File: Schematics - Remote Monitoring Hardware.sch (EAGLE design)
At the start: 48 parts, among them IC1 MSP430G2553, IC2 TPS77001, IC3 Xbee S3 Socket, IC4 MAX31855T, J5B PCC-SMP, J7 53047-06, Q1 32.768kHz, Q2 DMP3099L-7

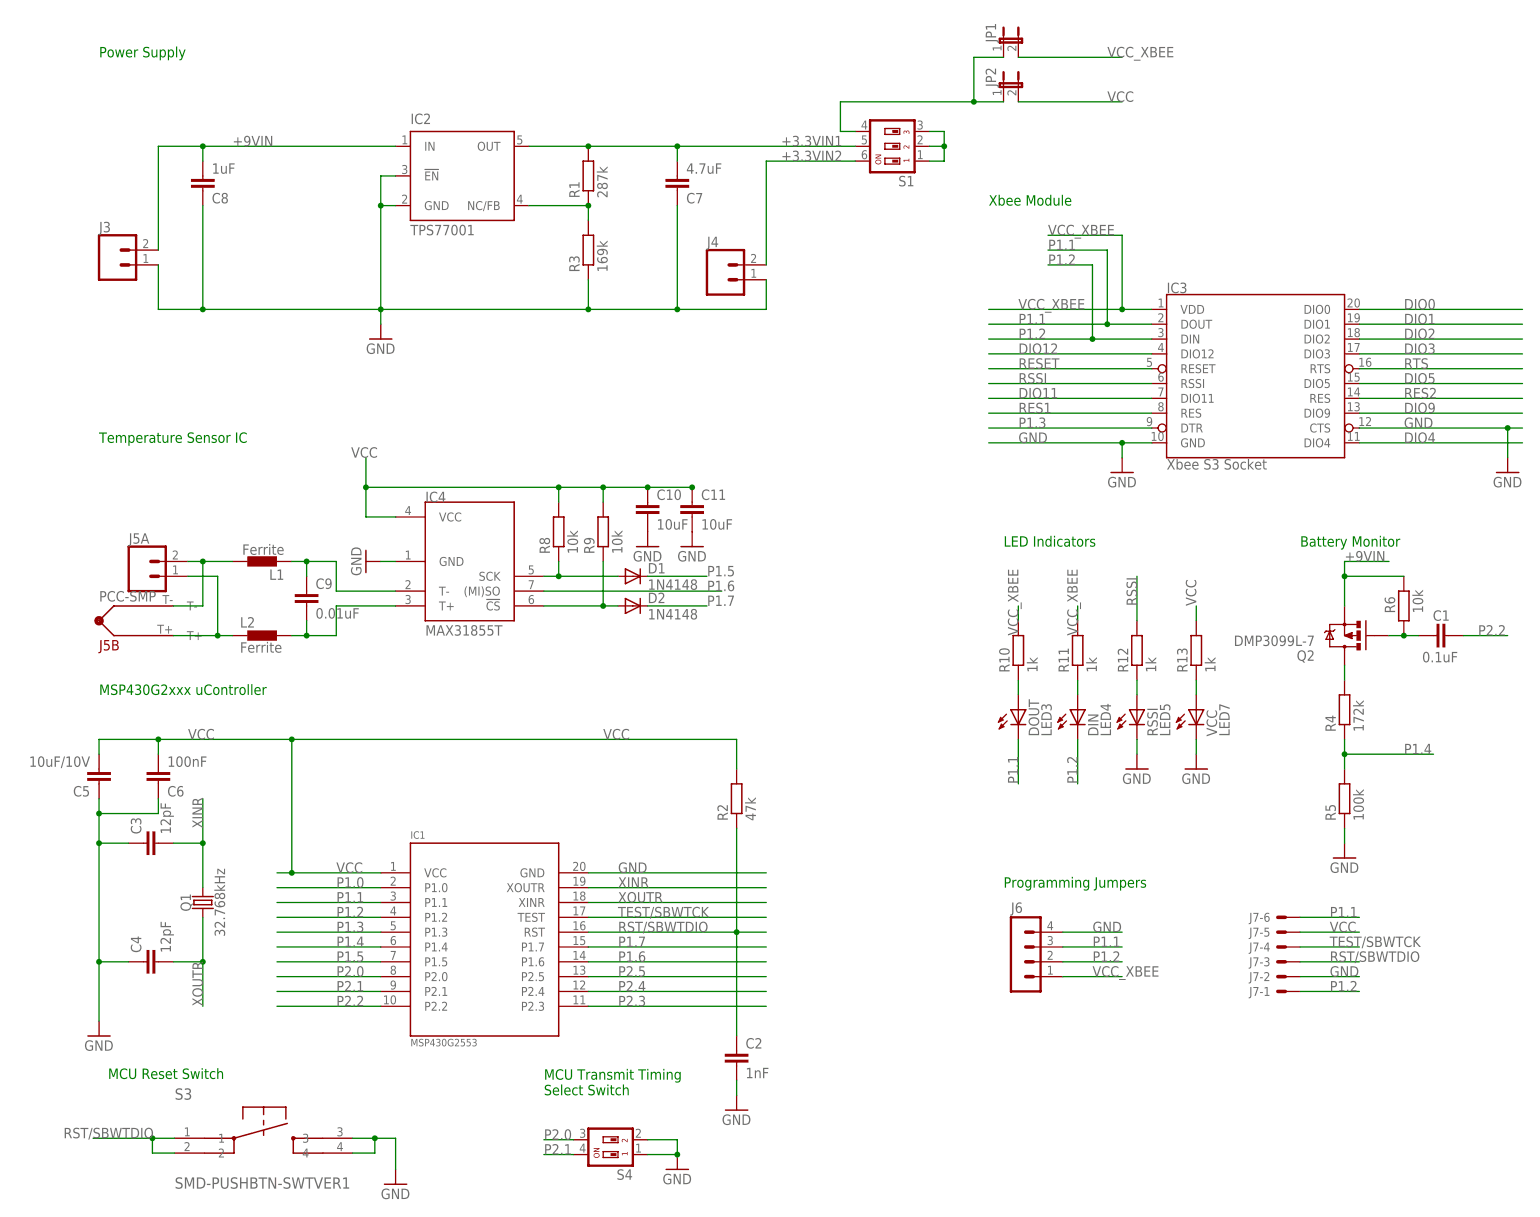
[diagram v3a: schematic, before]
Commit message: brd sch BOM changes Sept 20 2017
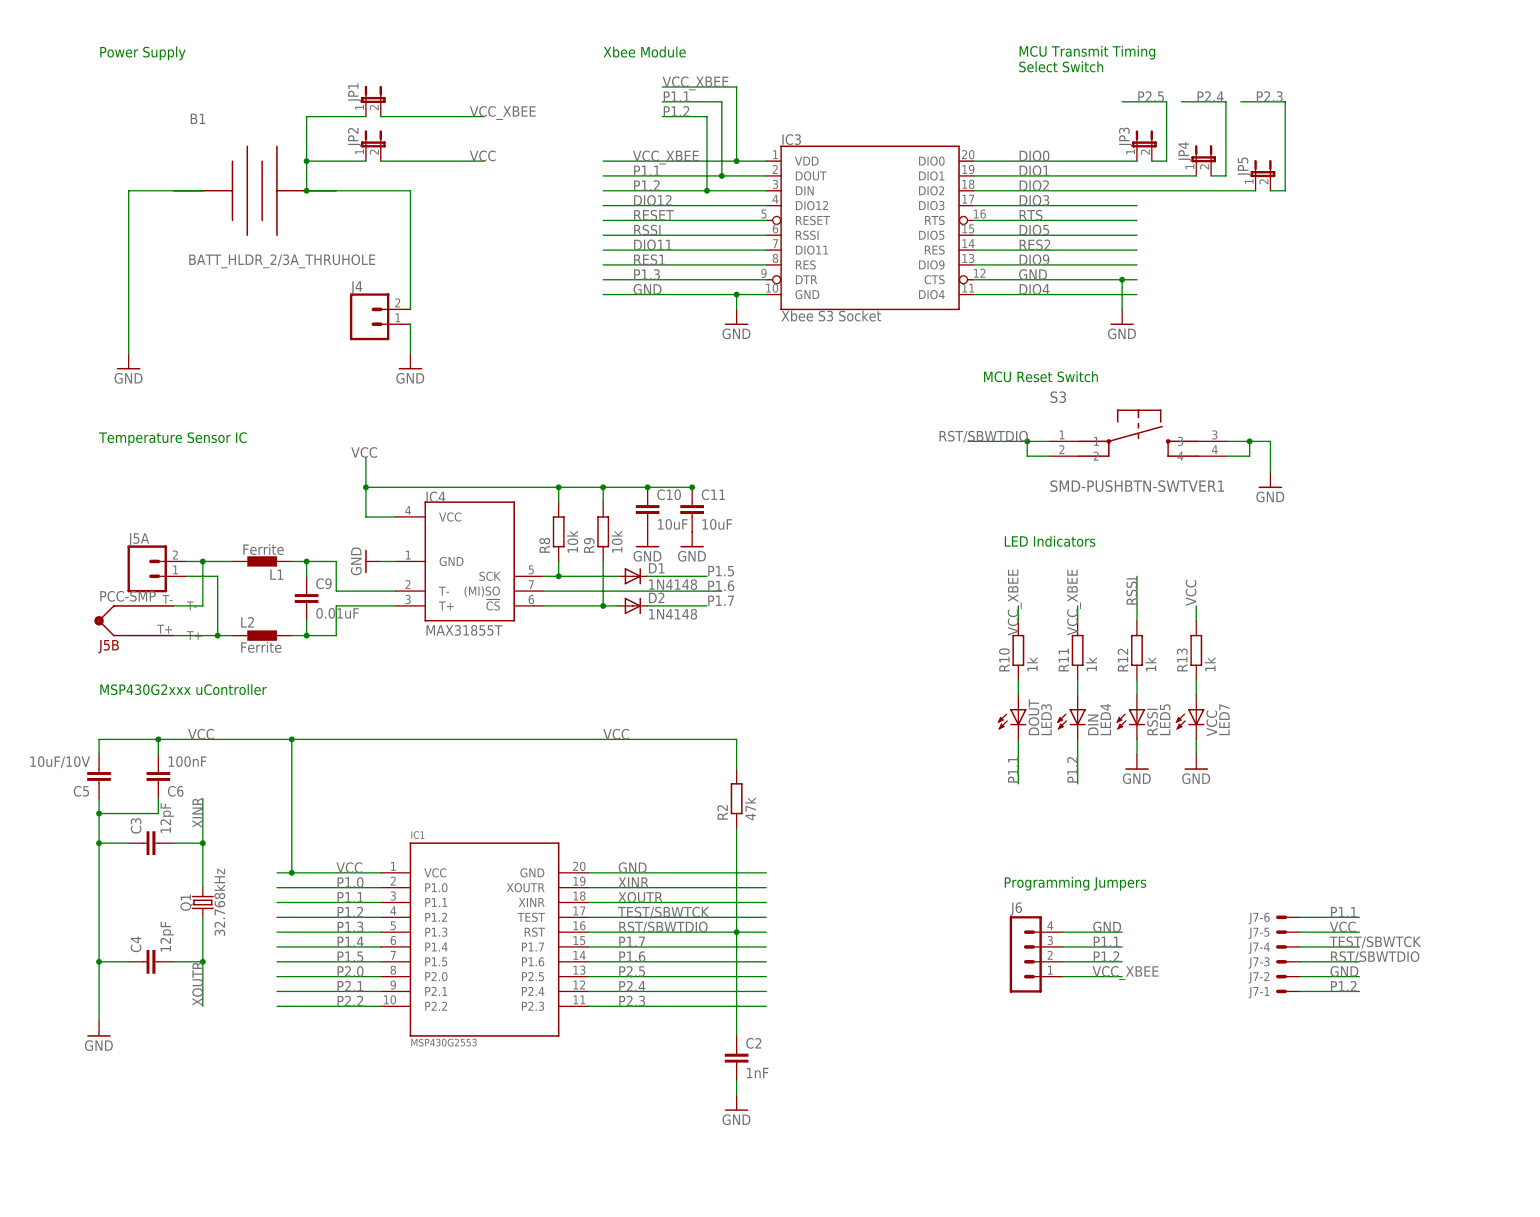
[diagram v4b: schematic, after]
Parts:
- removed C1: 0.1uF, eagle-ltspice:C
- removed C7: 4.7uF, eagle-ltspice:C
- removed C8: 1uF, eagle-ltspice:C
- removed IC2: TPS77001, texas:TPS77001
- removed J3: (no value), SparkFun-Connectors:CONN_023.5MM
- removed Q2: DMP3099L-7, User-Submitted:MOSFET-PCHANNELIRLML2244
- removed R1: 287k, eagle-ltspice:R
- removed R3: 169k, eagle-ltspice:R
- removed R4: 172k, eagle-ltspice:R
- removed R5: 100k, eagle-ltspice:R
- removed R6: 10k, eagle-ltspice:R
- removed S1: SWS003, smd-special:SWS003
- removed S4: SWS002, smd-special:SWS002
- added B1: BATT_HLDR_2/3A_THRUHOLE, custom parts:BATT_HLDR_2/3A_THRUHOLE
- added JP3, JP4, JP5: (no value), SparkFun-Retired:JUMPER-2PTH
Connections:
- removed net +3.3VIN1: C7.2, IC2.OUT, R1.2, S1.5
- removed net +3.3VIN2: J4.2, S1.6
- removed net +9VIN: C8.2, IC2.IN, J3.2, Q2.S, R6.2
- removed net N$16: JP1.1, JP2.1, S1.4
- removed net N$2: C1.2, Q2.G, R6.1
- removed net N$3: Q2.D, R4.2
- removed net N$5: IC2.NC/FB, R1.1, R3.2
- net DIO0: now also JP3.1
- net DIO1: now also JP4.1
- net DIO2: now also JP5.1
- net GND: now also B1.NEG; no longer C7.1, C8.1, IC2.!EN, IC2.GND, J3.1, R3.1, R5.1, S4.1, S4.2
- net N$1: now also B1.POS, J4.2, JP1.1, JP2.1; no longer S1.1, S1.2, S1.3
- net P1.4: no longer R4.1, R5.2
- net P2.0: no longer S4.3
- net P2.1: no longer S4.4
- net P2.2: no longer C1.1
- net P2.3: now also JP5.2
- net P2.4: now also JP4.2
- net P2.5: now also JP3.2
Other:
- note removed: "Battery Monitor"
- moved on the sheet: IC3, J4, JP1, JP2, S3
